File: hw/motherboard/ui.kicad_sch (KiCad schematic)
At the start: 10 parts, among them SW1 SW_Push, U1 RC1602A

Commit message: Updated page settings in schematic
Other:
- company: (none) -> DTUEliten
- title: (none) -> Irish Coffee Unlimited - Main
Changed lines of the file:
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@@
 (kicad_sch (version 20211123) (generator eeschema)
   (paper "A4")
+  (title_block
+    (title "Irish Coffee Unlimited - Main")
+    (date "2022-03-16")
+    (rev "1")
+    (company "DTUEliten")
+  )
   (junction (at 112.776 137.16) (diameter 0) (color 0 0 0 0)
   )

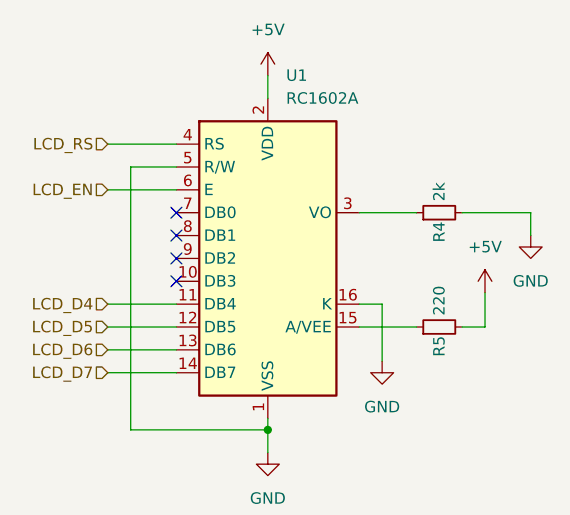
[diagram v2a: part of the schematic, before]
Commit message: Fixed DRC errors on schematic
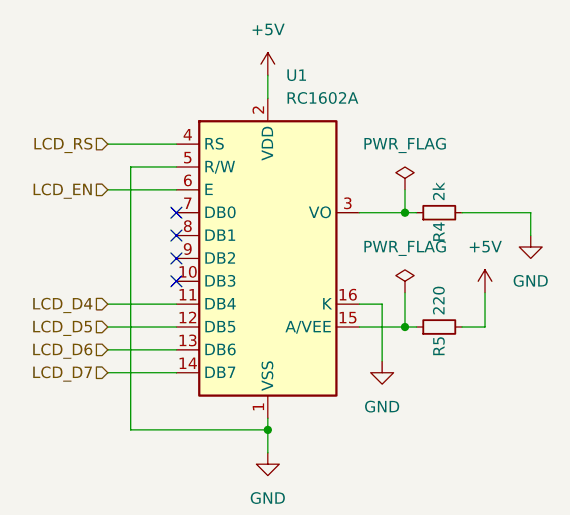
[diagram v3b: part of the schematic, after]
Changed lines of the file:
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@@
     (company "DTUEliten")
   )
+  (junction (at 143.51 64.77) (diameter 0) (color 0 0 0 0)
+  )
   (junction (at 112.776 137.16) (diameter 0) (color 0 0 0 0)
   )
@@
   )
   (junction (at 128.27 76.2) (diameter 0) (color 0 0 0 0)
+  )
+  (junction (at 143.51 52.07) (diameter 0) (color 0 0 0 0)
   )
   (junction (at 68.58 125.73) (diameter 0) (color 0 0 0 0)
@@
     (stroke (width 0) (type default) (color 0 0 0 0))
   )
-  (wire (pts (xy 138.43 64.77) (xy 144.78 64.77))
+  (wire (pts (xy 138.43 64.77) (xy 143.51 64.77))
     (stroke (width 0) (type default) (color 0 0 0 0))
   )
@@
     (stroke (width 0) (type default) (color 0 0 0 0))
   )
-  (wire (pts (xy 138.43 52.07) (xy 144.78 52.07))
+  (wire (pts (xy 138.43 52.07) (xy 143.51 52.07))
     (stroke (width 0) (type default) (color 0 0 0 0))
   )
@@
     (stroke (width 0) (type default) (color 0 0 0 0))
   )
+  (wire (pts (xy 143.51 52.07) (xy 144.78 52.07))
+    (stroke (width 0) (type default) (color 0 0 0 0))
+  )
   (wire (pts (xy 110.49 67.31) (xy 118.11 67.31))
     (stroke (width 0) (type default) (color 0 0 0 0))
@@
     (stroke (width 0) (type default) (color 0 0 0 0))
   )
+  (wire (pts (xy 143.51 64.77) (xy 144.78 64.77))
+    (stroke (width 0) (type default) (color 0 0 0 0))
+  )
   (wire (pts (xy 109.22 119.38) (xy 106.68 119.38))
     (stroke (width 0) (type default) (color 0 0 0 0))
@@
     (stroke (width 0) (type default) (color 0 0 0 0))
   )
+  (wire (pts (xy 143.51 49.53) (xy 143.51 52.07))
+    (stroke (width 0) (type default) (color 0 0 0 0))
+  )
   (wire (pts (xy 149.86 52.07) (xy 157.48 52.07))
     (stroke (width 0) (type default) (color 0 0 0 0))
   )
   (wire (pts (xy 112.776 137.16) (xy 112.776 139.573))
+    (stroke (width 0) (type default) (color 0 0 0 0))
+  )
+  (wire (pts (xy 143.51 60.96) (xy 143.51 64.77))
     (stroke (width 0) (type default) (color 0 0 0 0))
   )
@@
     )
     (property "Datasheet" "" (id 3) (at 73.66 139.7 0)
+      (effects (font (size 1.27 1.27)) hide)
+    )
+    (pin "1")
+  )
+  (symbol (lib_id "power:PWR_FLAG") (at 143.51 49.53 0) (unit 1)
+    (in_bom yes) (on_board yes) (fields_autoplaced)
+    (property "Reference" "#FLG0105" (id 0) (at 143.51 47.625 0)
+      (effects (font (size 1.27 1.27)) hide)
+    )
+    (property "Value" "PWR_FLAG" (id 1) (at 143.51 44.45 0))
+    (property "Footprint" "" (id 2) (at 143.51 49.53 0)
+      (effects (font (size 1.27 1.27)) hide)
+    )
+    (property "Datasheet" "~" (id 3) (at 143.51 49.53 0)
       (effects (font (size 1.27 1.27)) hide)
     )
@@
       (effects (font (size 1.27 1.27)) hide)
     )
+    (pin "1")
+  )
+  (symbol (lib_id "power:PWR_FLAG") (at 143.51 60.96 0) (unit 1)
+    (in_bom yes) (on_board yes) (fields_autoplaced)
+    (property "Reference" "#FLG0104" (id 0) (at 143.51 59.055 0)
+      (effects (font (size 1.27 1.27)) hide)
+    )
+    (property "Value" "PWR_FLAG" (id 1) (at 143.51 55.88 0))
+    (property "Footprint" "" (id 2) (at 143.51 60.96 0)
+      (effects (font (size 1.27 1.27)) hide)
+    )
+    (property "Datasheet" "~" (id 3) (at 143.51 60.96 0)
+      (effects (font (size 1.27 1.27)) hide)
+    )

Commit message: Fixed footprints for alle components
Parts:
- C3: footprint (none) -> Capacitor_SMD:C_0402_1005Metric_Pad0.74x0.62mm_HandSolder
- R1: footprint (none) -> Resistor_SMD:R_0402_1005Metric_Pad0.72x0.64mm_HandSolder
- R2, R3, R4, R5: footprint Resistor_SMD:R_0805_2012Metric -> Resistor_SMD:R_0402_1005Metric_Pad0.72x0.64mm_HandSolder
- SW1: footprint (none) -> Connector_PinHeader_2.54mm:PinHeader_1x02_P2.54mm_Vertical
- U1: footprint Display:RC1602A -> Connector_PinHeader_2.54mm:PinHeader_1x16_P2.54mm_Vertical
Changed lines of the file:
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@@
       (effects (font (size 1.27 1.27)) (justify left))
     )
-    (property "Footprint" "" (id 2) (at 73.66 120.65 0)
+    (property "Footprint" "Resistor_SMD:R_0402_1005Metric_Pad0.72x0.64mm_HandSolder" (id 2) (at 73.66 120.65 0)
       (effects (font (size 1.27 1.27)) hide)
     )
@@
       (effects (font (size 1.27 1.27)) (justify left))
     )
-    (property "Footprint" "" (id 2) (at 78.74 132.08 0)
+    (property "Footprint" "Connector_PinHeader_2.54mm:PinHeader_1x02_P2.54mm_Vertical" (id 2) (at 78.74 132.08 0)
       (effects (font (size 1.27 1.27)) hide)
     )
@@
       (effects (font (size 1.27 1.27)) (justify left))
     )
-    (property "Footprint" "Resistor_SMD:R_0805_2012Metric" (id 2) (at 147.32 52.07 0)
+    (property "Footprint" "Resistor_SMD:R_0402_1005Metric_Pad0.72x0.64mm_HandSolder" (id 2) (at 147.32 52.07 0)
       (effects (font (size 1.27 1.27)) hide)
     )
@@
       (effects (font (size 1.27 1.27)) (justify left))
     )
-    (property "Footprint" "Display:RC1602A" (id 2) (at 130.81 77.47 0)
+    (property "Footprint" "Connector_PinHeader_2.54mm:PinHeader_1x16_P2.54mm_Vertical" (id 2) (at 130.81 77.47 0)
       (effects (font (size 1.27 1.27)) hide)
     )
@@
       (effects (font (size 1.27 1.27)) (justify left))
     )
-    (property "Footprint" "Resistor_SMD:R_0805_2012Metric" (id 2) (at 116.84 123.19 0)
+    (property "Footprint" "Resistor_SMD:R_0402_1005Metric_Pad0.72x0.64mm_HandSolder" (id 2) (at 116.84 123.19 0)
       (effects (font (size 1.27 1.27)) hide)
     )
@@
       (effects (font (size 1.27 1.27)) (justify left))
     )
-    (property "Footprint" "" (id 2) (at 68.58 130.81 0)
+    (property "Footprint" "Capacitor_SMD:C_0402_1005Metric_Pad0.74x0.62mm_HandSolder" (id 2) (at 68.58 130.81 0)
       (effects (font (size 1.27 1.27)) hide)
     )
@@
       (effects (font (size 1.27 1.27)) (justify left))
     )
-    (property "Footprint" "Resistor_SMD:R_0805_2012Metric" (id 2) (at 147.32 64.77 0)
+    (property "Footprint" "Resistor_SMD:R_0402_1005Metric_Pad0.72x0.64mm_HandSolder" (id 2) (at 147.32 64.77 0)
       (effects (font (size 1.27 1.27)) hide)
     )
@@
       (effects (font (size 1.27 1.27)) (justify left))
     )
-    (property "Footprint" "Resistor_SMD:R_0805_2012Metric" (id 2) (at 109.22 124.46 0)
-      (effects (font (size 1.27 1.27)) hide)
-    )
+    (property "Footprint" "Resistor_SMD:R_0402_1005Metric_Pad0.72x0.64mm_HandSolder" (id 2) (at 109.22 124.46 0)
+      (effects (font (size 1.27 1.27)) hide)
+    )
